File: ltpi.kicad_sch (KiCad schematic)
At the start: 1 part, among them J2 PinHeader_2x10_P1.27mm_SMD_Sh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

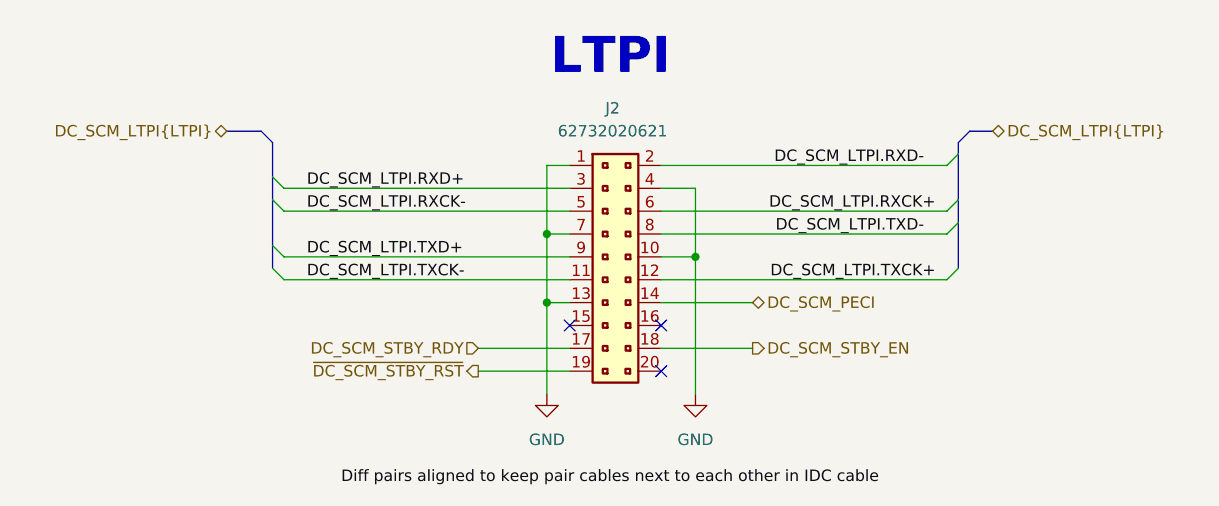
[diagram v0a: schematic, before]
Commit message: [#92504] Connect QWIIC connector
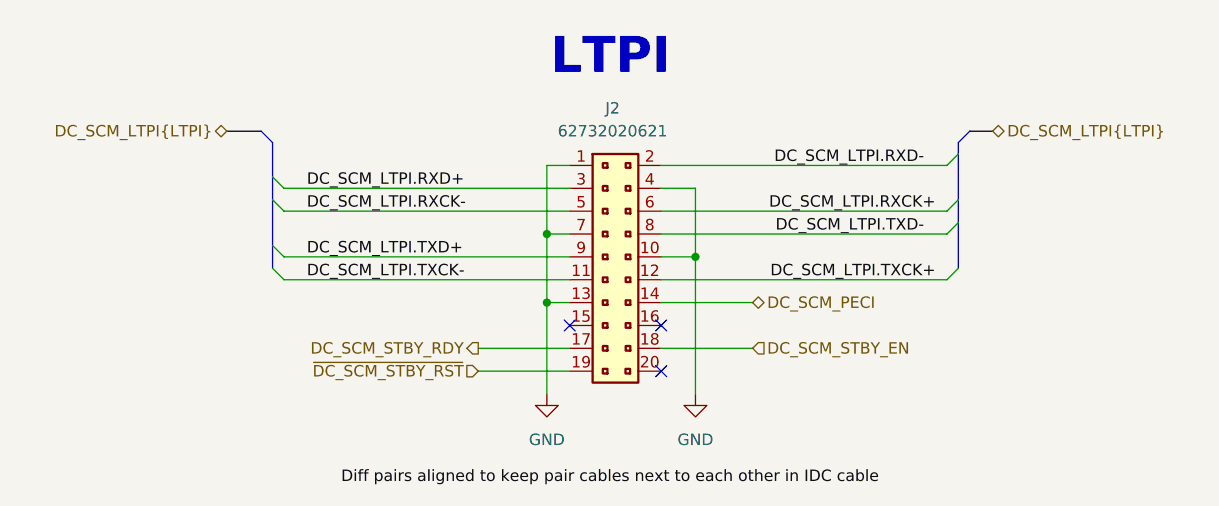
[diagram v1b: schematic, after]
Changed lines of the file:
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@@
 	)
 	(hierarchical_label "DC_SCM_STBY_EN"
-		(shape output)
+		(shape input)
 		(at 90.17 57.15 0)
 		(effects
@@
 	)
 	(hierarchical_label "~{DC_SCM_STBY_RST}"
-		(shape output)
+		(shape input)
 		(at 59.69 59.69 180)
 		(effects
@@
 	)
 	(hierarchical_label "DC_SCM_STBY_RDY"
-		(shape input)
+		(shape output)
 		(at 59.69 57.15 180)
 		(effects
@@
 					(unit 1)
 				)
-				(path "/5d67ef28-5805-4f87-b722-2926dabf7f6e/d9b5a36f-f960-4ce7-8269-f56a658e52fc"
-					(reference "J2")
-					(unit 1)
-				)
 			)
 		)
@@
 					(unit 1)
 				)
-				(path "/5d67ef28-5805-4f87-b722-2926dabf7f6e/d9b5a36f-f960-4ce7-8269-f56a658e52fc"
-					(reference "#PWR026")
-					(unit 1)
-				)
 			)
 		)
@@
 					(unit 1)
 				)
-				(path "/5d67ef28-5805-4f87-b722-2926dabf7f6e/d9b5a36f-f960-4ce7-8269-f56a658e52fc"
-					(reference "#PWR027")
-					(unit 1)
-				)

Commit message: [#92504] Clear Wire BUS errors
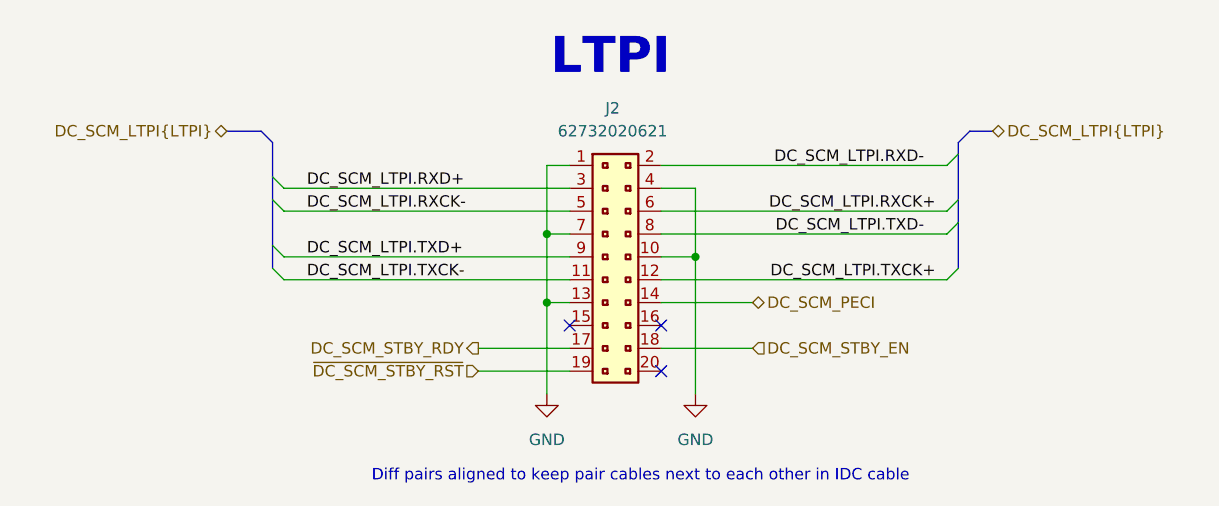
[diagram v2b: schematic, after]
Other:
- note added: "Diff pairs aligned to keep pair cables next to each other in IDC cable"
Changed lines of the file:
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@@
+		)
+	)
+	(text "Diff pairs aligned to keep pair cables next to each other in IDC cable\n"
+		(exclude_from_sim no)
+		(at 77.724 71.374 0)
+		(effects
+			(font
+				(size 1.27 1.27)
+			)
 		)
 	)
@@
 		(effects
 			(font
-				(size 1.27 1.27)
-			)
-			(justify left bottom)
-		)
-	)
-	(label "Diff pairs aligned to keep pair cables next to each other in IDC cable"
-		(at 44.45 72.39 0)
-		(effects
-			(font

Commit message: [#92504] Update Annotation for connectors
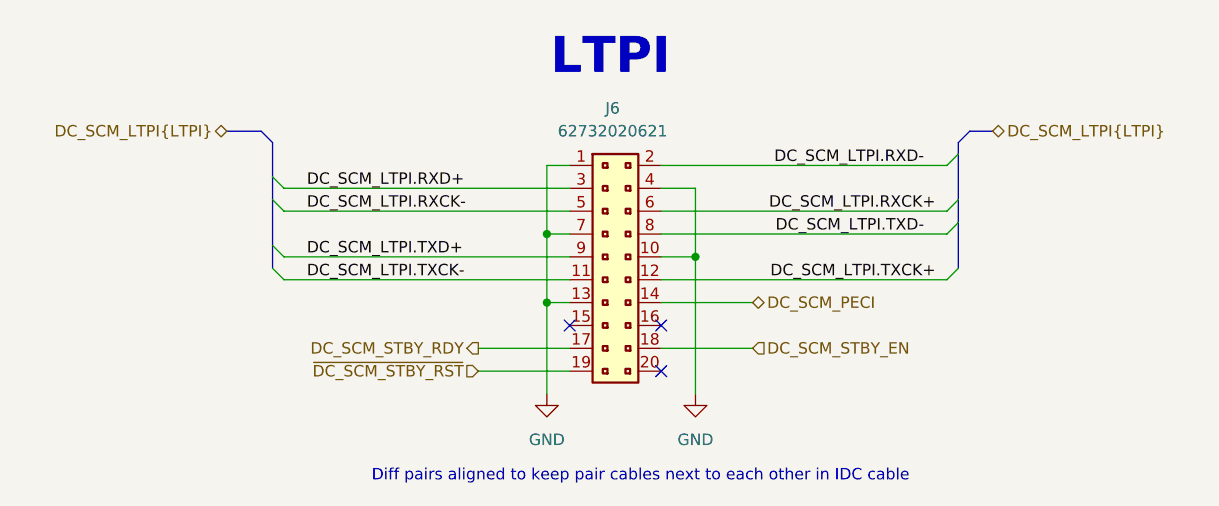
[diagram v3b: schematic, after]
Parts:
- renumbered J2 to J6
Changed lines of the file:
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@@
 		(dnp no)
 		(fields_autoplaced yes)
-		(property "Reference" "J2"
+		(property "Reference" "J6"
 			(at 74.6125 30.48 0)
 			(effects
@@
 			(project ""
 				(path "/5d67ef28-5805-4f87-b722-2926dabf7f6e/71f72096-b015-4537-aa01-1b933a065d45"
-					(reference "J2")
+					(reference "J6")
 					(unit 1)
 				)
